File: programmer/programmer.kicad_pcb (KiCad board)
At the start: 2 copper layers, 40 x 20 mm, 21 parts, among them J1 10118192-0001LF, J2 Conn_02x05_Odd_Even, Q1 Q_NMOS_GSD, Q2 Q_NMOS_GSD, U1 TLV75533PDBV, U2 FT2232HL, U3 ASDMB-12.000MHz

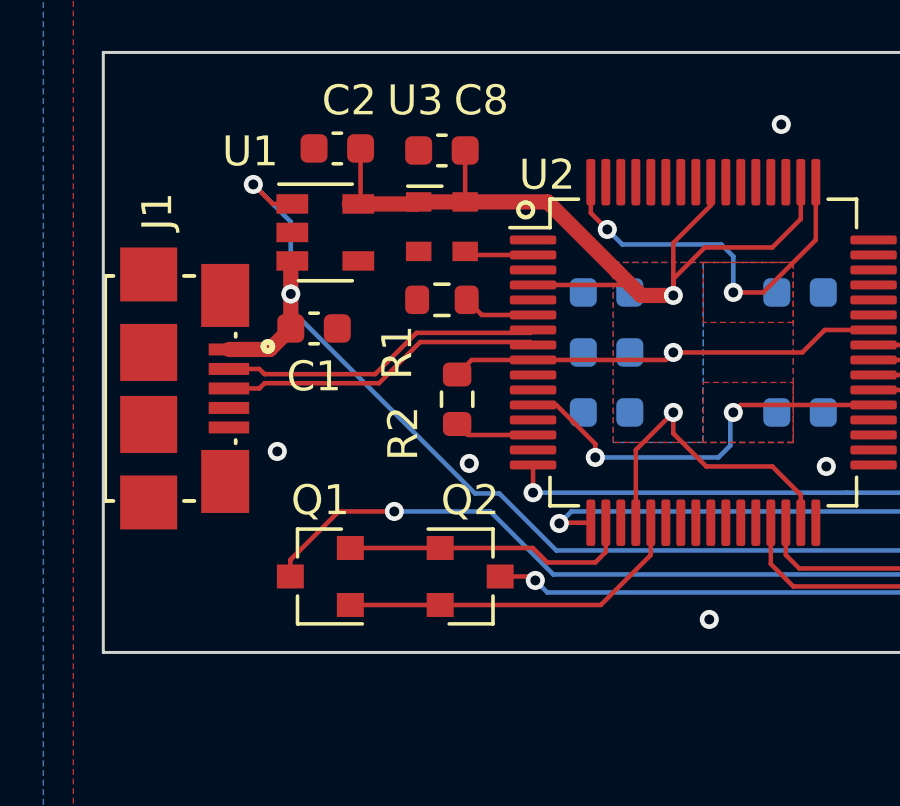
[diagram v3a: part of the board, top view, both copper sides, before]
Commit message: Finished version 2 of programmer, now with JTAG
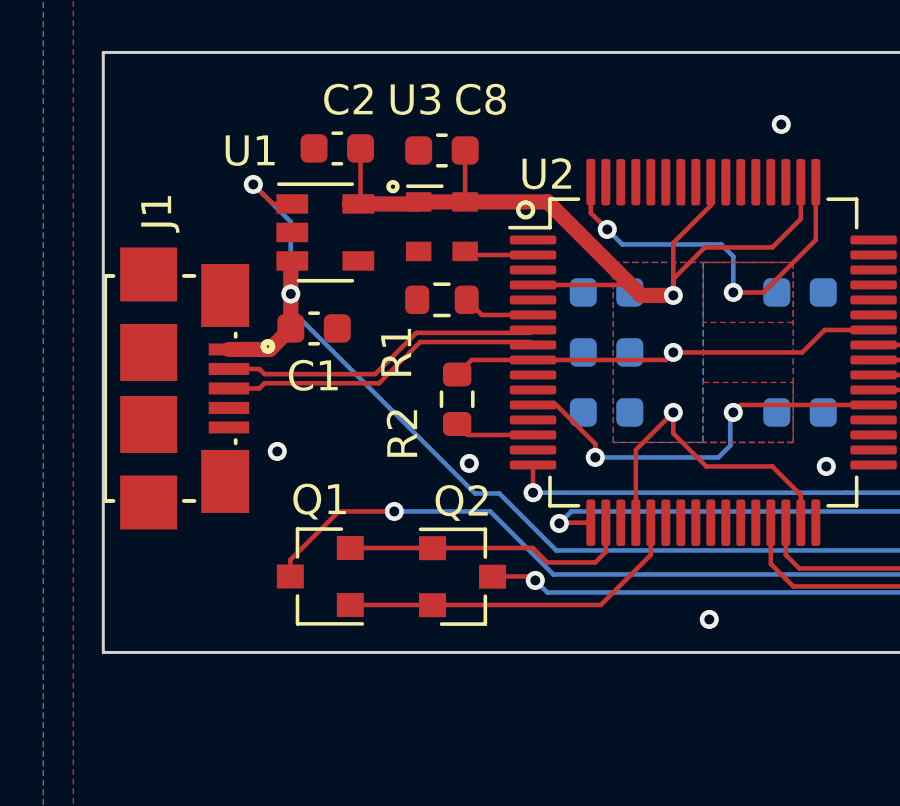
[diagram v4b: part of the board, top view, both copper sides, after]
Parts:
- C3: value 3.3uF -> 1uF
- J2: value Conn_02x05_Odd_Even -> 3220-10-0100-00
- Q1, Q2: value Q_NMOS_GSD -> 2N7002ET1G
- moved Q2 0.25 mm to (-8.03, 7.47)
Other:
- rule pad_to_mask_clearance: 0.051 -> 0
